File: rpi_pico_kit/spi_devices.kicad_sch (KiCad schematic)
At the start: 44 parts, among them J6 Micro_SD_Card_Det, SW10 SW, SW3 SW, SW4 SW, SW5 SW, SW6 SW, SW7 SW, SW8 SW, SW9 SW, U5 74LS165, U6 74LS595

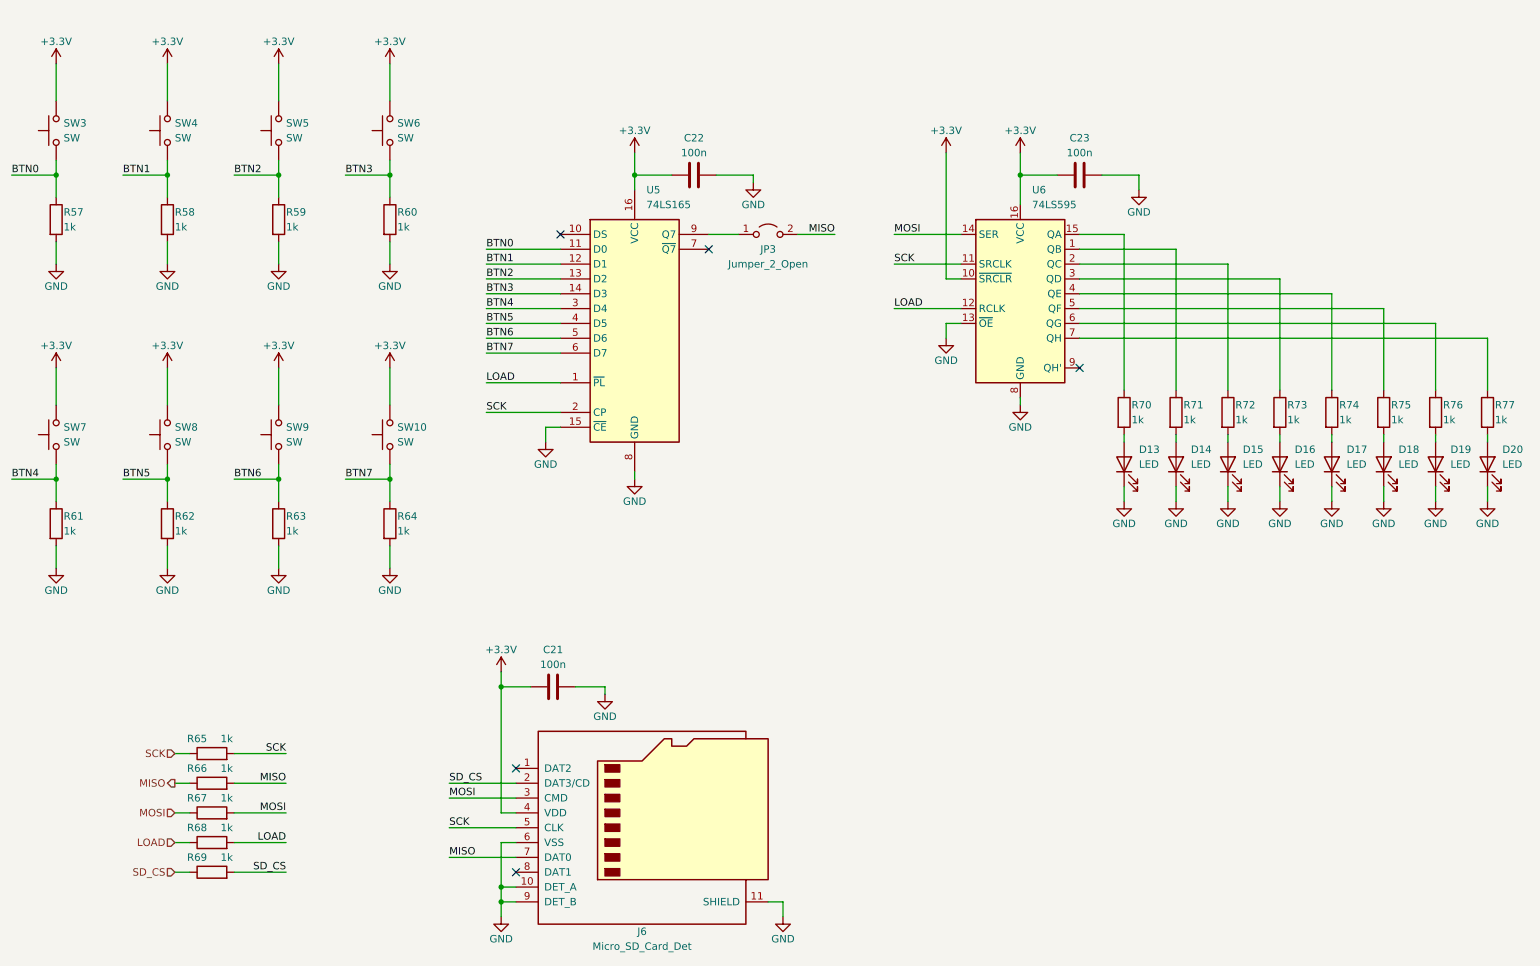
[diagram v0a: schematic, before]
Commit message: replaced spi expander
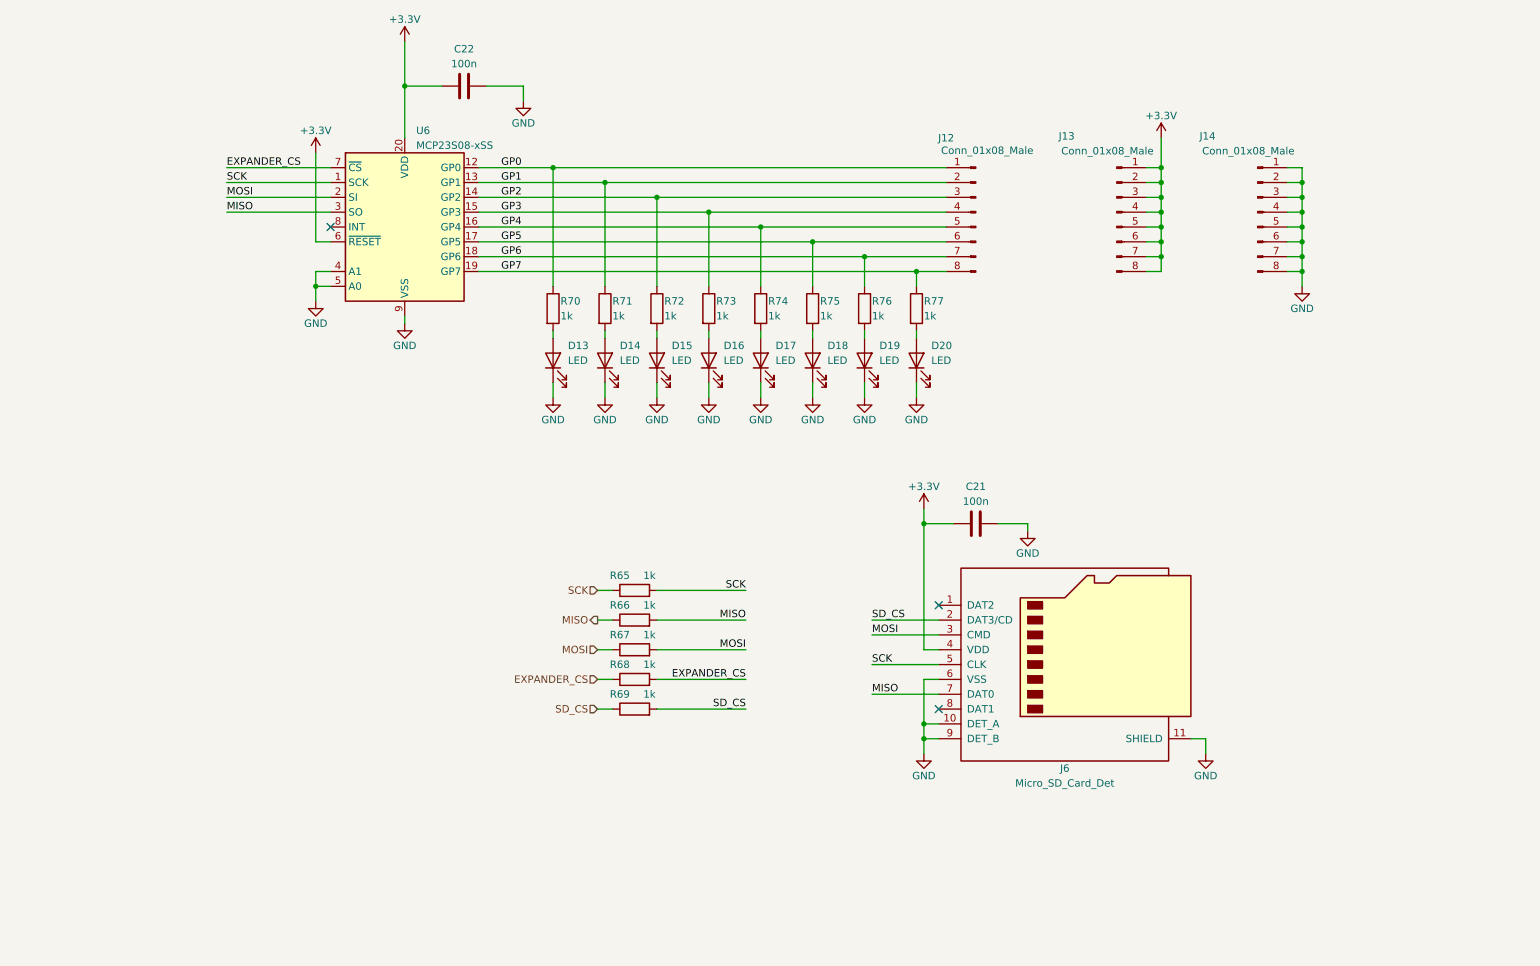
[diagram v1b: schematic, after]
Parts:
- removed C23: 100n, Capacitor_SMD:C_0805_2012Metric_Pad1.18x1.45mm_HandSolder, symbol Device:C
- removed JP3: Jumper_2_Open, TestPoint:TestPoint_2Pads_Pitch2.54mm_Drill0.8mm, symbol Jumper:Jumper_2_Open
- removed R57, R58, R59, R60, R61, R62, R63, R64: 1k, Resistor_SMD:R_0805_2012Metric_Pad1.20x1.40mm_HandSolder, symbol Device:R
- removed SW10, SW3, SW4, SW5, SW6, SW7, SW8, SW9: SW, symbol Switch:SW_Push
- removed U5: 74LS165, Package_SO:SOIC-16_3.9x9.9mm_P1.27mm, symbol 74xx:74LS165
- removed U6: 74LS595, Package_SO:SOIC-16_3.9x9.9mm_P1.27mm, symbol 74xx:74LS595
- added J12, J13, J14: Conn_01x08_Male, Connector_PinHeader_2.54mm:PinHeader_1x08_P2.54mm_Vertical, symbol Connector:Conn_01x08_Male
- added U6: MCP23S08-xSS, Package_SO:SSOP-20_5.3x7.2mm_P0.65mm, symbol Interface_Expansion:MCP23S08-xSS
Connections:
- net +3V3: now also J13.1 (Pin_1), J13.2 (Pin_2), J13.3 (Pin_3), J13.4 (Pin_4), J13.5 (Pin_5), J13.6 (Pin_6), J13.7 (Pin_7), J13.8 (Pin_8), U6.20 (VDD), U6.6 (~{RESET})
- net GND: now also J14.1 (Pin_1), J14.2 (Pin_2), J14.3 (Pin_3), J14.4 (Pin_4), J14.5 (Pin_5), J14.6 (Pin_6), J14.7 (Pin_7), J14.8 (Pin_8), U6.4 (A1), U6.5 (A0), U6.9 (VSS)
- net MISO: now also U6.3 (SO)
- net MOSI: now also U6.2 (SI)
- net SCK: now also U6.1 (SCK)
- net GP5: now reaches R75.1
- net GP5: now also J12.6 (Pin_6), U6.17 (GP5)
- net GP6: now reaches R76.1
- net GP6: now also J12.7 (Pin_7), U6.18 (GP6)
- net GP0: now reaches R70.1
- net GP0: now also J12.1 (Pin_1), U6.12 (GP0)
- net GP4: now reaches R74.1
- net GP4: now also J12.5 (Pin_5), U6.16 (GP4)
- net GP3: now reaches R73.1
- net GP3: now also J12.4 (Pin_4), U6.15 (GP3)
- net GP1: now reaches R71.1
- net GP1: now also J12.2 (Pin_2), U6.13 (GP1)
- net GP2: now reaches R72.1
- net GP2: now also J12.3 (Pin_3), U6.14 (GP2)
- net GP7: now reaches R77.1
- net GP7: now also J12.8 (Pin_8), U6.19 (GP7)
- net LOAD renamed EXPANDER_CS
- net EXPANDER_CS: now also U6.7 (~{CS})
- no-connect marks 5 -> 3
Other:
- moved on the sheet: C21, D13, D14, D15, D16, D17, D18, D19, D20, J6, R65, R66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

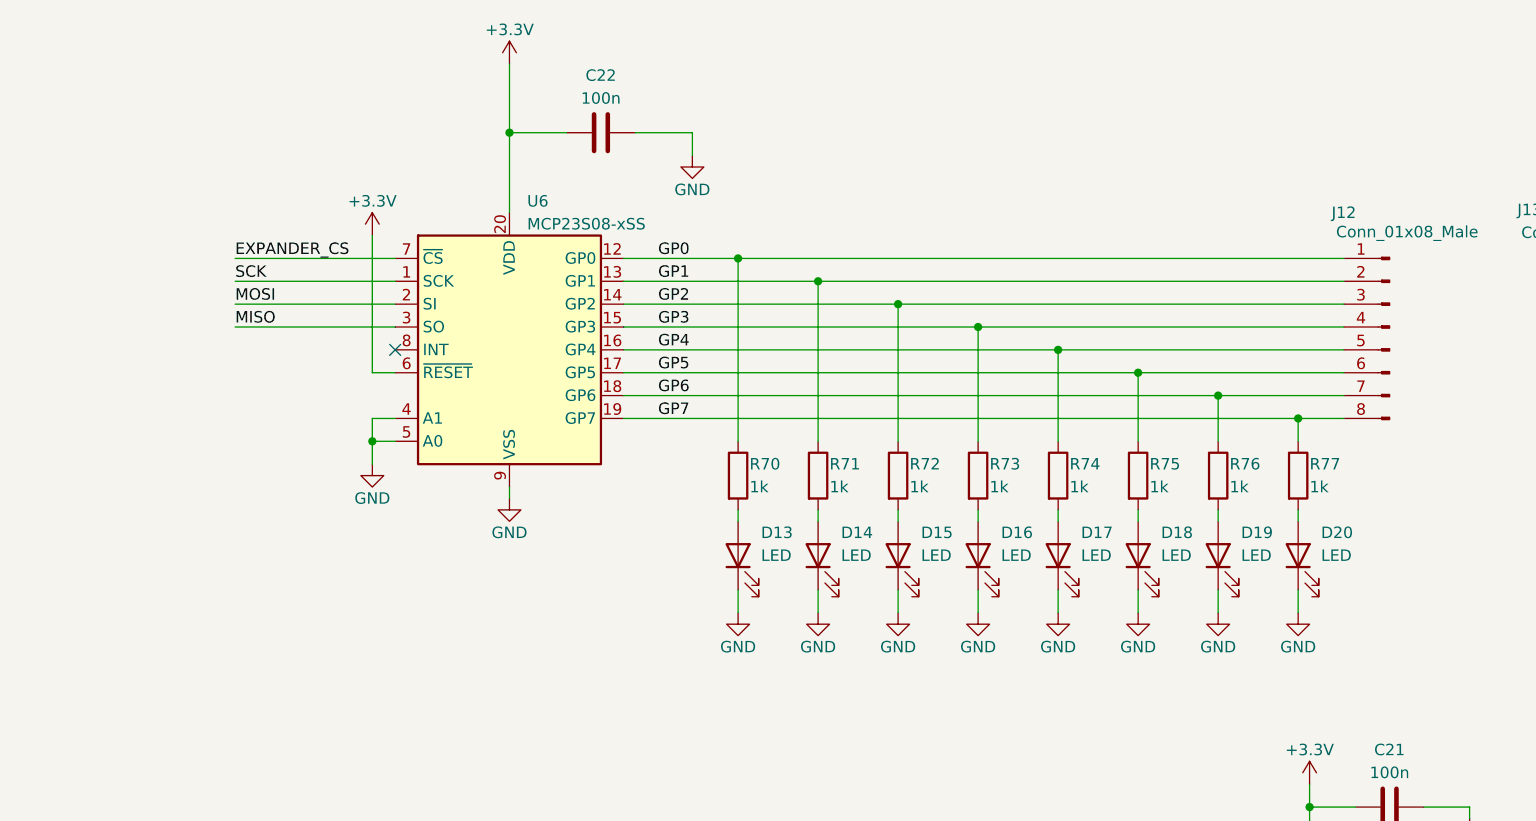
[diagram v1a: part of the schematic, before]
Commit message: added resistors to expander's buttons
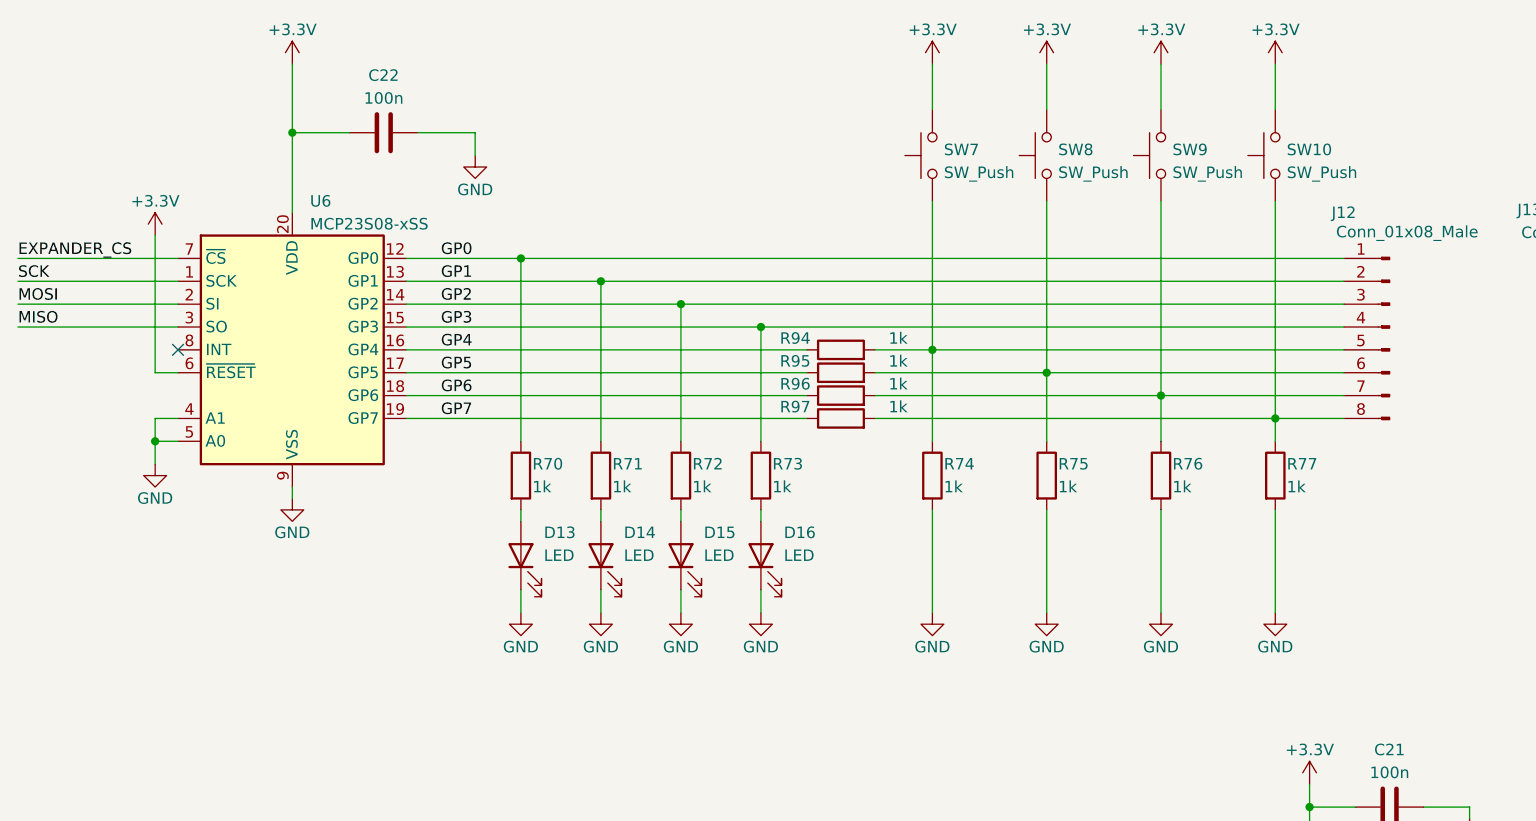
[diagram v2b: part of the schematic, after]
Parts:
- removed D17, D18, D19, D20: LED, LED_SMD:LED_1206_3216Metric_Pad1.42x1.75mm_HandSolder, symbol Device:LED
- added R94, R95, R96, R97: 1k, Resistor_SMD:R_0805_2012Metric_Pad1.20x1.40mm_HandSolder, symbol Device:R
- added SW10, SW7, SW8, SW9: SW_Push, Button_Switch_THT:SW_TH_Tactile_Omron_B3F-10xx, symbol Switch:SW_Push
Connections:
- net +3V3: now also SW10.2, SW7.2, SW8.2, SW9.2
- net GND: now also R74.2, R75.2, R76.2, R77.2
- net GP4: now also R94.1; no longer J12.5 (Pin_5), R74.1
- net GP5: now also R95.1; no longer J12.6 (Pin_6), R75.1
- net GP6: now also R96.1; no longer J12.7 (Pin_7), R76.1
- net GP7: now also R97.1; no longer J12.8 (Pin_8), R77.1
- new net: J12.6 (Pin_6), R75.1, R95.2, SW8.1
- new net: J12.8 (Pin_8), R77.1, R97.2, SW10.1
- new net: J12.5 (Pin_5), R74.1, R94.2, SW7.1
- new net: J12.7 (Pin_7), R76.1, R96.2, SW9.1
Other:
- moved on the sheet: C22, D13, D14, D15, D16, R70, R71, R72, R73, R74, R75, R76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

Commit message: added some footprints
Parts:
- D13, D14, D15, D16: footprint LED_SMD:LED_1206_3216Metric_Pad1.42x1.75mm_HandSolder -> LED_SMD:LED_0805_2012Metric_Pad1.15x1.40mm_HandSolder
- U6: footprint Package_SO:SSOP-20_5.3x7.2mm_P0.65mm -> (none)
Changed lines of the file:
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@@
       (effects (font (size 1.27 1.27)) (justify right))
     )
-    (property "Footprint" "LED_SMD:LED_1206_3216Metric_Pad1.42x1.75mm_HandSolder" (id 2) (at 96.52 82.55 0)
+    (property "Footprint" "LED_SMD:LED_0805_2012Metric_Pad1.15x1.40mm_HandSolder" (id 2) (at 96.52 82.55 0)
       (effects (font (size 1.27 1.27)) hide)
     )
@@
       (effects (font (size 1.27 1.27)) (justify right))
     )
-    (property "Footprint" "LED_SMD:LED_1206_3216Metric_Pad1.42x1.75mm_HandSolder" (id 2) (at 114.3 82.55 0)
+    (property "Footprint" "LED_SMD:LED_0805_2012Metric_Pad1.15x1.40mm_HandSolder" (id 2) (at 114.3 82.55 0)
       (effects (font (size 1.27 1.27)) hide)
     )
@@
       (effects (font (size 1.27 1.27)) (justify left))
     )
-    (property "Footprint" "Package_SO:SSOP-20_5.3x7.2mm_P0.65mm" (id 2) (at 62.23 86.36 0)
+    (property "Footprint" "" (id 2) (at 62.23 86.36 0)
       (effects (font (size 1.27 1.27)) hide)
     )
@@
       (effects (font (size 1.27 1.27)) (justify right))
     )
-    (property "Footprint" "LED_SMD:LED_1206_3216Metric_Pad1.42x1.75mm_HandSolder" (id 2) (at 87.63 82.55 0)
+    (property "Footprint" "LED_SMD:LED_0805_2012Metric_Pad1.15x1.40mm_HandSolder" (id 2) (at 87.63 82.55 0)
       (effects (font (size 1.27 1.27)) hide)
     )
@@
       (effects (font (size 1.27 1.27)) (justify right))
     )
-    (property "Footprint" "LED_SMD:LED_1206_3216Metric_Pad1.42x1.75mm_HandSolder" (id 2) (at 105.41 82.55 0)
-      (effects (font (size 1.27 1.27)) hide)
-    )
+    (property "Footprint" "LED_SMD:LED_0805_2012Metric_Pad1.15x1.40mm_HandSolder" (id 2) (at 105.41 82.55 0)
+      (effects (font (size 1.27 1.27)) hide)
+    )

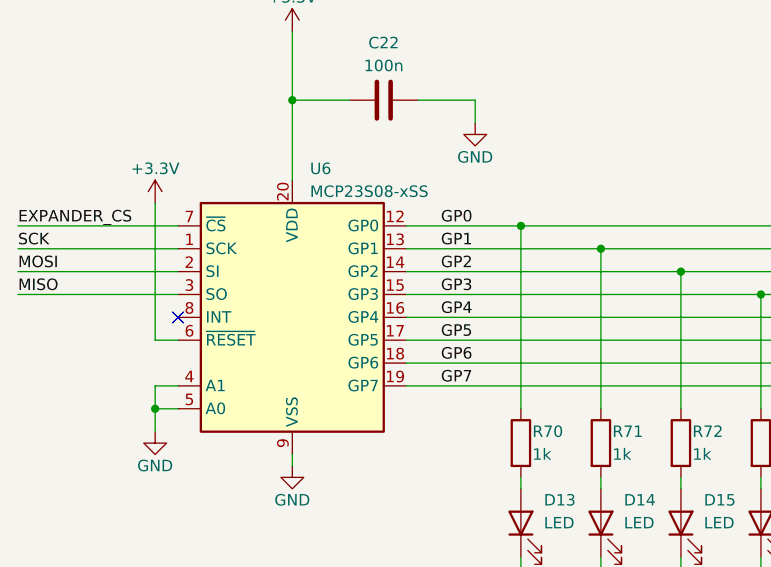
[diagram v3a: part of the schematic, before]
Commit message: edited 5V I2C, added some footprints, MPNs, added HDMI footprint library
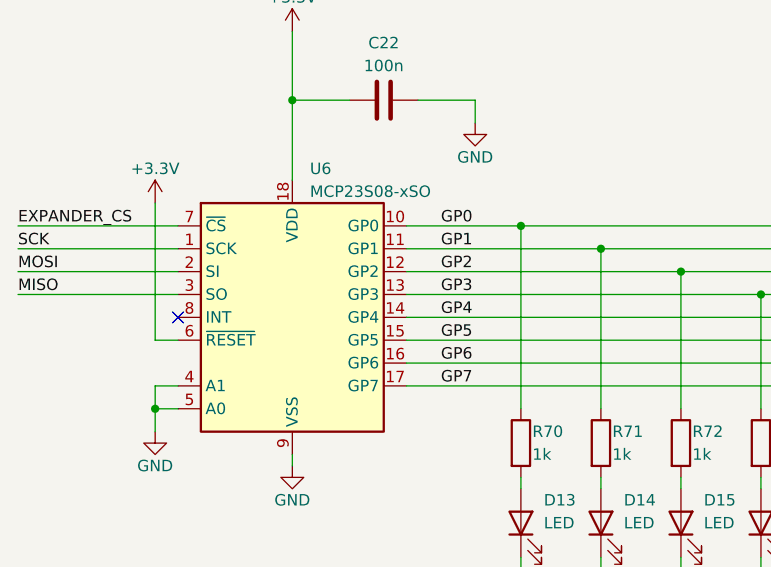
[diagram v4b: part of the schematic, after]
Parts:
- removed U6: MCP23S08-xSS, symbol Interface_Expansion:MCP23S08-xSS
- added U6: MCP23S08-xSO, Package_SO:SOIC-18W_7.5x11.6mm_P1.27mm, symbol Interface_Expansion:MCP23S08-xSO
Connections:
- net +3V3: now also U6.18 (VDD), U6.6 (~{RESET})
- net EXPANDER_CS: now also U6.7 (~{CS})
- net GND: now also U6.4 (A1), U6.5 (A0), U6.9 (VSS)
- net GP0: now also U6.10 (GP0)
- net GP1: now also U6.11 (GP1)
- net GP2: now also U6.12 (GP2)
- net GP3: now also U6.13 (GP3)
- net GP4: now also U6.14 (GP4)
- net GP5: now also U6.15 (GP5)
- net GP6: now also U6.16 (GP6)
- net GP7: now also U6.17 (GP7)
- net MISO: now also U6.3 (SO)
- net MOSI: now also U6.2 (SI)
- net SCK: now also U6.1 (SCK)
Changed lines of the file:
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@@
     (pin "1")
-  )
-  (symbol (lib_id "Interface_Expansion:MCP23S08-xSS") (at 62.23 59.69 0) (unit 1)
-    (in_bom yes) (on_board yes) (fields_autoplaced)
-    (property "Reference" "U6" (id 0) (at 64.1859 43.18 0)
-      (effects (font (size 1.27 1.27)) (justify left))
-    )
-    (property "Value" "MCP23S08-xSS" (id 1) (at 64.1859 45.72 0)
-      (effects (font (size 1.27 1.27)) (justify left))
-    )
-    (property "Footprint" "" (id 2) (at 62.23 86.36 0)
-      (effects (font (size 1.27 1.27)) hide)
-    )
-    (property "Datasheet" "http://ww1.microchip.com/downloads/en/DeviceDoc/MCP23008-MCP23S08-Data-Sheet-20001919F.pdf" (id 3) (at 95.25 90.17 0)
-      (effects (font (size 1.27 1.27)) hide)
-    )
-    (pin "1")
-    (pin "10")
-    (pin "11")
-    (pin "12")
-    (pin "13")
-    (pin "14")
-    (pin "15")
-    (pin "16")
-    (pin "17")
-    (pin "18")
-    (pin "19")
-    (pin "2")
-    (pin "20")
-    (pin "3")
-    (pin "4")
-    (pin "5")
-    (pin "6")
-    (pin "7")
-    (pin "8")
-    (pin "9")
   )
   (symbol (lib_id "Device:R") (at 123.19 62.23 90) (unit 1)
@@
     (pin "1")
   )
+  (symbol (lib_name "MCP23S08-xSO_1") (lib_id "Interface_Expansion:MCP23S08-xSO") (at 62.23 59.69 0) (unit 1)
+    (in_bom yes) (on_board yes) (fields_autoplaced)
+    (property "Reference" "U6" (id 0) (at 64.1859 43.18 0)
+      (effects (font (size 1.27 1.27)) (justify left))
+    )
+    (property "Value" "MCP23S08-xSO" (id 1) (at 64.1859 45.72 0)
+      (effects (font (size 1.27 1.27)) (justify left))
+    )
+    (property "Footprint" "Package_SO:SOIC-18W_7.5x11.6mm_P1.27mm" (id 2) (at 62.23 86.36 0)
+      (effects (font (size 1.27 1.27)) hide)
+    )
+    (property "Datasheet" "http://ww1.microchip.com/downloads/en/DeviceDoc/MCP23008-MCP23S08-Data-Sheet-20001919F.pdf" (id 3) (at 95.25 90.17 0)
+      (effects (font (size 1.27 1.27)) hide)
+    )
+    (property "Manufacturer Part Number" "MCP23S08-E/SO" (id 4) (at 62.23 59.69 0)
+      (effects (font (size 1.27 1.27)) hide)
+    )
+    (property "Supplier" "Digikey" (id 5) (at 62.23 59.69 0)
+      (effects (font (size 1.27 1.27)) hide)
+    )
+    (property "Supplier Part URL" "https://www.digikey.cz/en/products/detail/microchip-technology/MCP23S08-E-SO/735955" (id 6) (at 62.23 59.69 0)
+      (effects (font (size 1.27 1.27)) hide)
+    )
+    (pin "1")
+    (pin "10")
+    (pin "11")
+    (pin "12")
+    (pin "13")
+    (pin "14")
+    (pin "15")
+    (pin "16")
+    (pin "17")
+    (pin "18")
+    (pin "2")
+    (pin "3")
+    (pin "4")
+    (pin "5")
+    (pin "6")
+    (pin "7")
+    (pin "8")
+    (pin "9")
+  )
   (symbol (lib_id "Connector:Conn_01x08_Male") (at 184.15 57.15 0) (mirror y) (unit 1)
